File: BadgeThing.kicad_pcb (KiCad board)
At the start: 2 copper layers, 78.7 x 40.2 mm, 65 parts, among them J1 USB_C_Receptacle_USB2.0, J2 Connector_Generic_Conn_01x02, J3 Ext 5V, J4 SWD Header, SW1 BOOTSEL, SW2 ESP RESET, SW3 Left, SW4 Down, SW5 Select, SW6 Up, SW7 Right, U2 W25Q32JVSS, U3 RP2040, U4 NCP1117-3.3_SOT223, U5 ESP-12F, Y1 12.000MHz

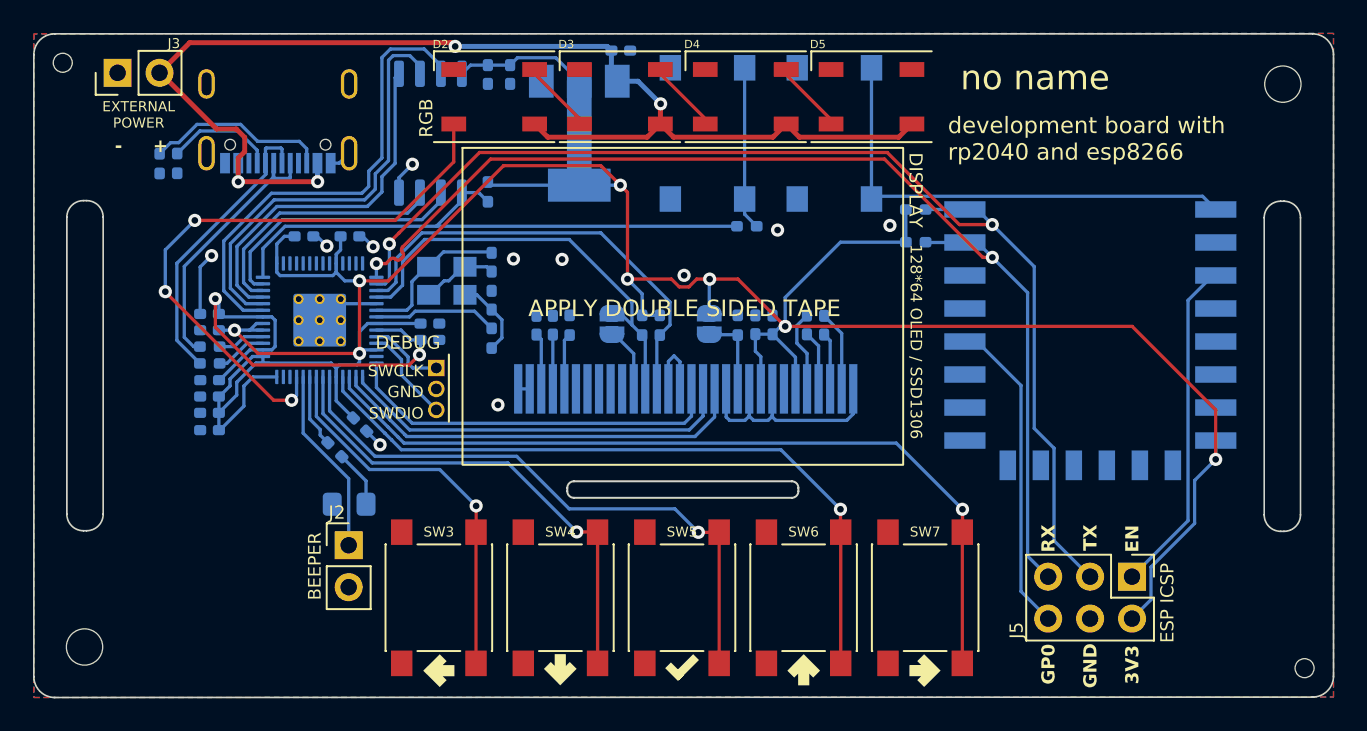
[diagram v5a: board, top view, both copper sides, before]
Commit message: Final board layout, up to first production order
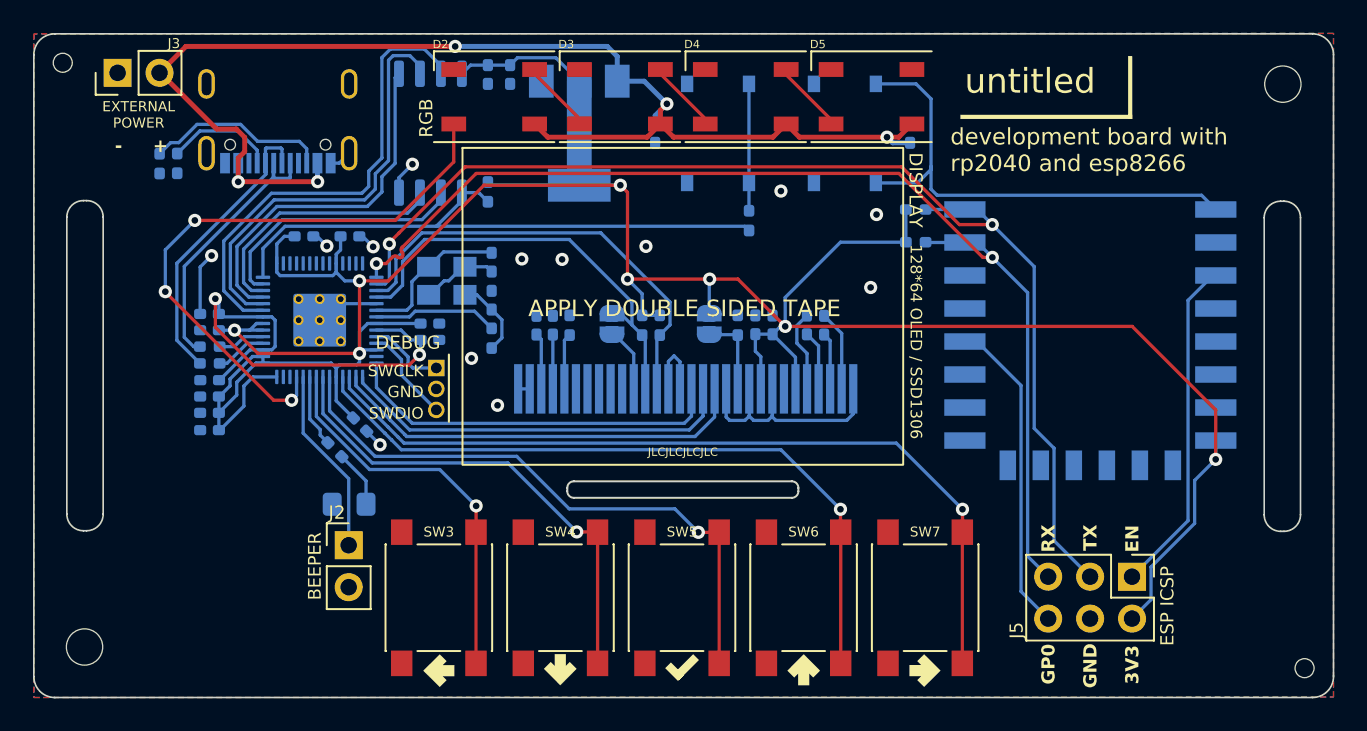
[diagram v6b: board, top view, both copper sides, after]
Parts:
- added C23: beeg, Capacitor_SMD:C_0402_1005Metric_Pad0.74x0.62mm_HandSolder, B.Cu at (175.5, 99.9)
- R2: value 390K -> 270k
- SW1, SW2: footprint Button_Switch_SMD:SW_Push_1P1T_NO_6x6mm_H9.5mm -> Button_Switch_SMD:SW_Push_1P1T_XKB_TS-1187A
- moved C16 5.44 mm to (160.1, 99.9), turned to -90 degrees
- moved SW1 0.64 mm to (163.9, 99.9)
- moved SW2 0.64 mm to (171.6, 99.9)
- moved R3 0.37 mm to (165.8, 105.2), turned to -90 degrees
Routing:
- net +5V: track 76.2 -> 79.6 mm, vias 4 -> 5
- net Net-(R3-Pad1): track 9.90 -> 7.69 mm
- net Net-(U5-~{RST}): track 29.2 -> 30.8 mm
- net +3V3: track 189.8 -> 188.4 mm
- net QSPI_SS: track 35.3 -> 36.3 mm
- net ESP_RX: track 68.9 -> 68.1 mm
- net ESP_TX: track 71.9 -> 71.2 mm
- net GND: vias 11 -> 13
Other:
- board text added: "JLCJLCJLCJLC"
- board text added: "mounting holes - m2 wristband slots - 20mm"
- board text added: "untitled"
- board text removed: "no name"

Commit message: 3V3 input + small tweaks
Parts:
- added J6: External 3V3, Connector_PinHeader_2.54mm:PinHeader_1x02_P2.54mm_Vertical, F.Cu at (194.0, 126.7)
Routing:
- net +3V3: track 188.4 -> 193.6 mm
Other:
- board text added: "EXTERNAL +3V3"
- board text added: "EXTERNAL +5V"
- board text removed: "EXTERNAL POWER"

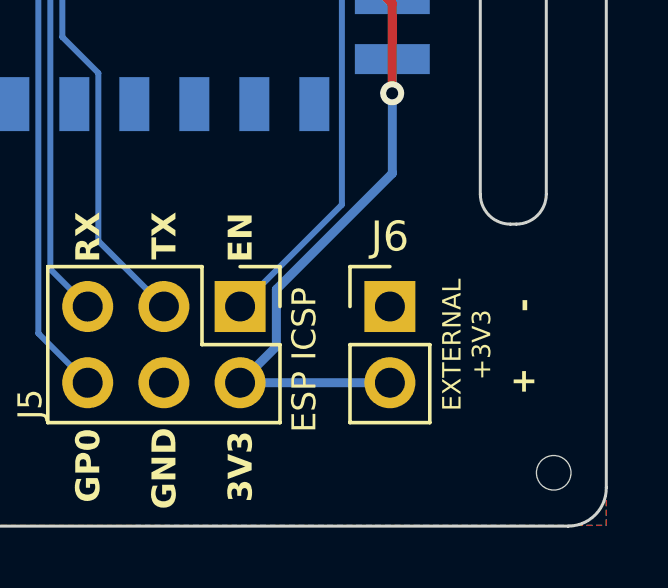
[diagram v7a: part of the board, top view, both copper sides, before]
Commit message: Align 3V3 input with ESP header at 2.54mm pitch
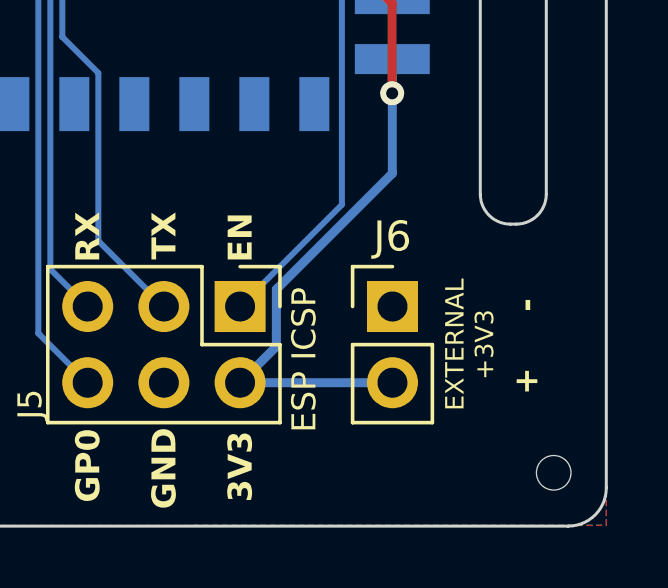
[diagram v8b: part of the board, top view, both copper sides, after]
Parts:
- moved J6 0.09 mm to (194.0, 126.7)
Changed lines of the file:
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@@
   )
   (footprint "Connector_PinHeader_2.54mm:PinHeader_1x02_P2.54mm_Vertical" (layer "F.Cu")
-    (at 193.9544 126.741)
+    (at 194.041 126.741)
     (descr "Through hole straight pin header, 1x02, 2.54mm pitch, single row")
     (tags "Through hole pin header THT 1x02 2.54mm single row")
@@
     (effects (font (size 0.8 0.8) (thickness 0.2) bold) (justify left))
   )
-  (gr_text "+" (at 198.3994 129.2352 90) (layer "F.SilkS")
+  (gr_text "+" (at 198.4996 129.229199 90) (layer "F.SilkS")
     (effects (font (size 0.8 0.8) (thickness 0.2) bold))
   )
@@
     (effects (font (size 0.8 0.8) (thickness 0.15)) (justify left bottom))
   )
-  (gr_text "EXTERNAL\n+3V3" (at 196.5198 128.016001 90) (layer "F.SilkS" knockout)
+  (gr_text "EXTERNAL\n+3V3" (at 196.62 128.01 90) (layer "F.SilkS" knockout)
     (effects (font (size 0.614 0.614) (thickness 0.15)))
   )
-  (gr_text "-" (at 198.3994 126.6952 90) (layer "F.SilkS")
+  (gr_text "-" (at 198.4996 126.689199 90) (layer "F.SilkS")
     (effects (font (size 0.8 0.8) (thickness 0.2) bold))
   )
